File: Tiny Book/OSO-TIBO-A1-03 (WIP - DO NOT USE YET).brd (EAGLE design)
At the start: 54.9 x 88.1 mm, 106 parts, among them J2 10118193-0001LF, Q1 DMG341, Q2 IRLML0100, SW1 SPST_TACTILE_SWITCHRA-THRU, SW2 SPDT_SWITCH, U1 AP2112-3.3, U2 MCP73831T-2ACI/OT, U3 ATSAMD51G18A-MUT, U4 GD25Q16C (or GD25Q32C), U5 MAX4468EKAT, X1 JSTPH, X2 2x5 0.05" SWD

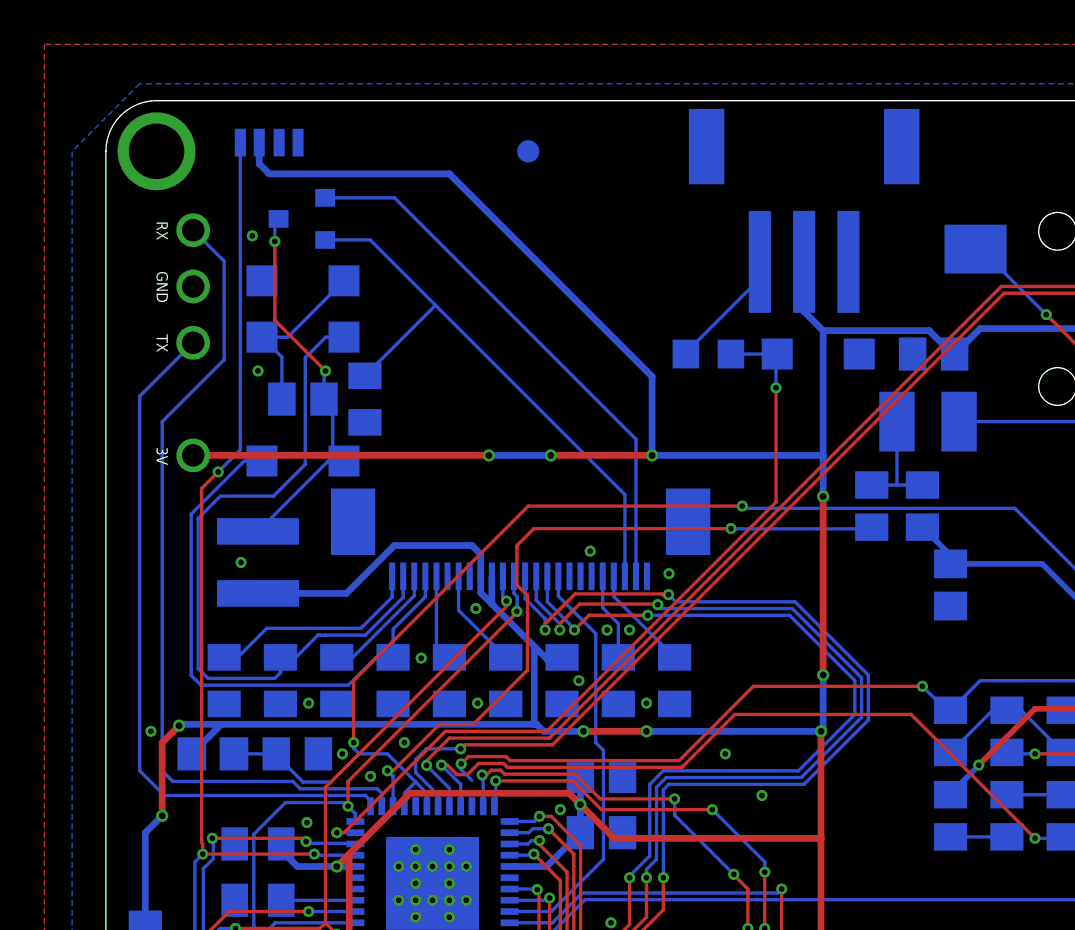
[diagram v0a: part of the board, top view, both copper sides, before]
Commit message: silkscreen and dimension tweaks
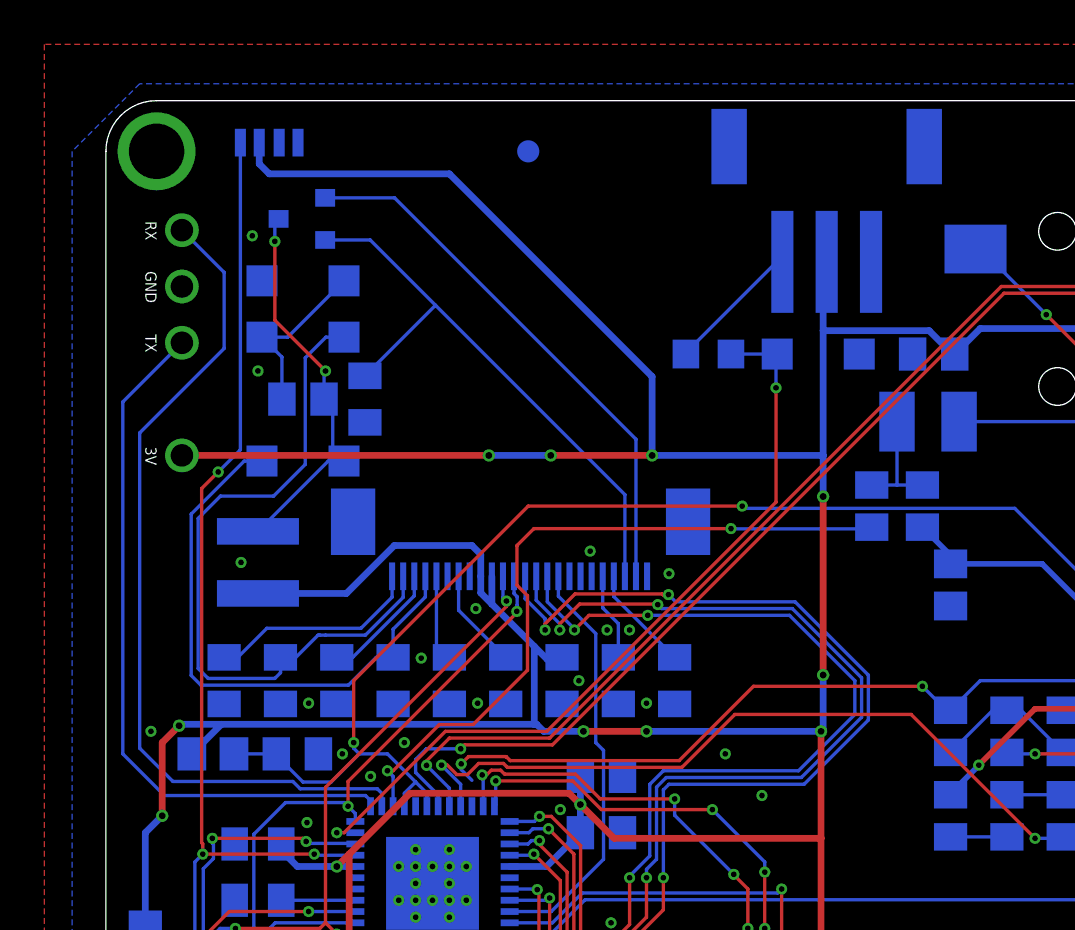
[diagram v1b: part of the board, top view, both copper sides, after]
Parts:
- moved ACCESSORY_PORT 1.02 mm to (32.5, 83.8)
- moved JP1 0.51 mm to (3.43, 80.0)
- moved JP2 0.51 mm to (3.43, 72.4)
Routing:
- net D0_SERCOM1_RX: track 37.0 -> 38.1 mm
- net _ACCESSORY: track 5.54 -> 6.11 mm
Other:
- board text added: "RX/TX=D1/D0=PA00/PA01"
- board text removed: "TX/RX=D1/D0=PA00/PA01"

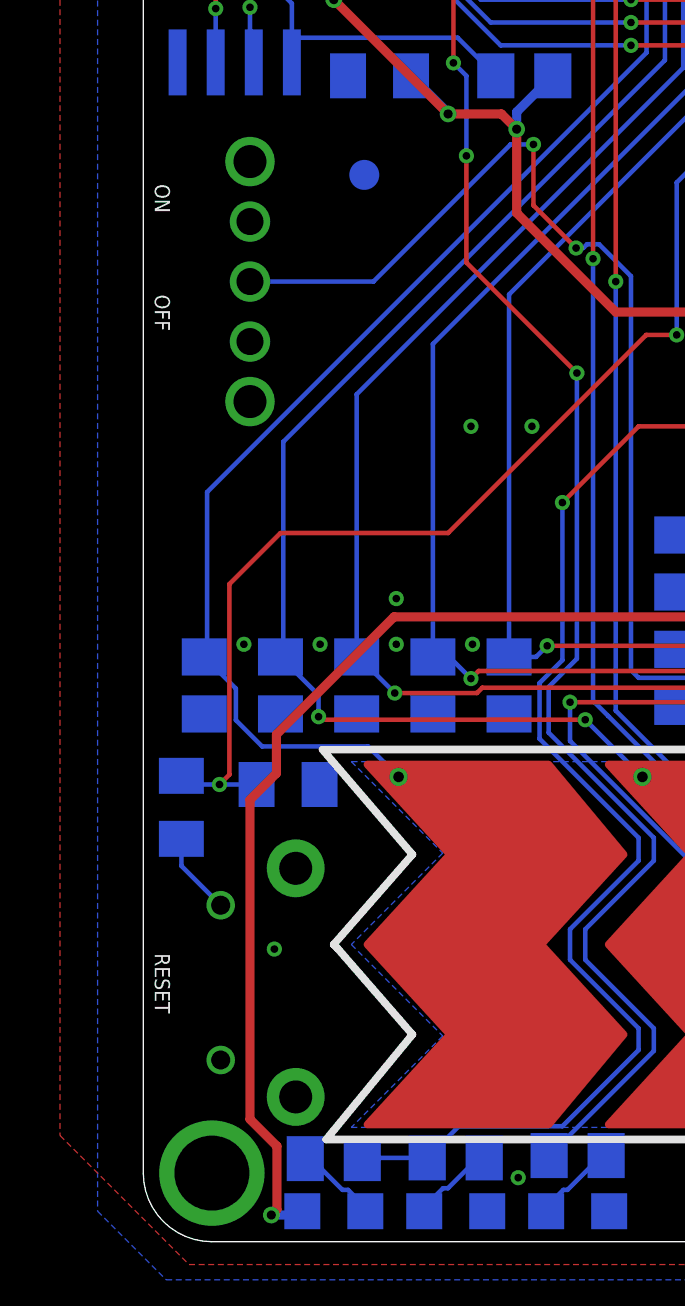
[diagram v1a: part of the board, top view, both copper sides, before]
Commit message: surface mount reset button
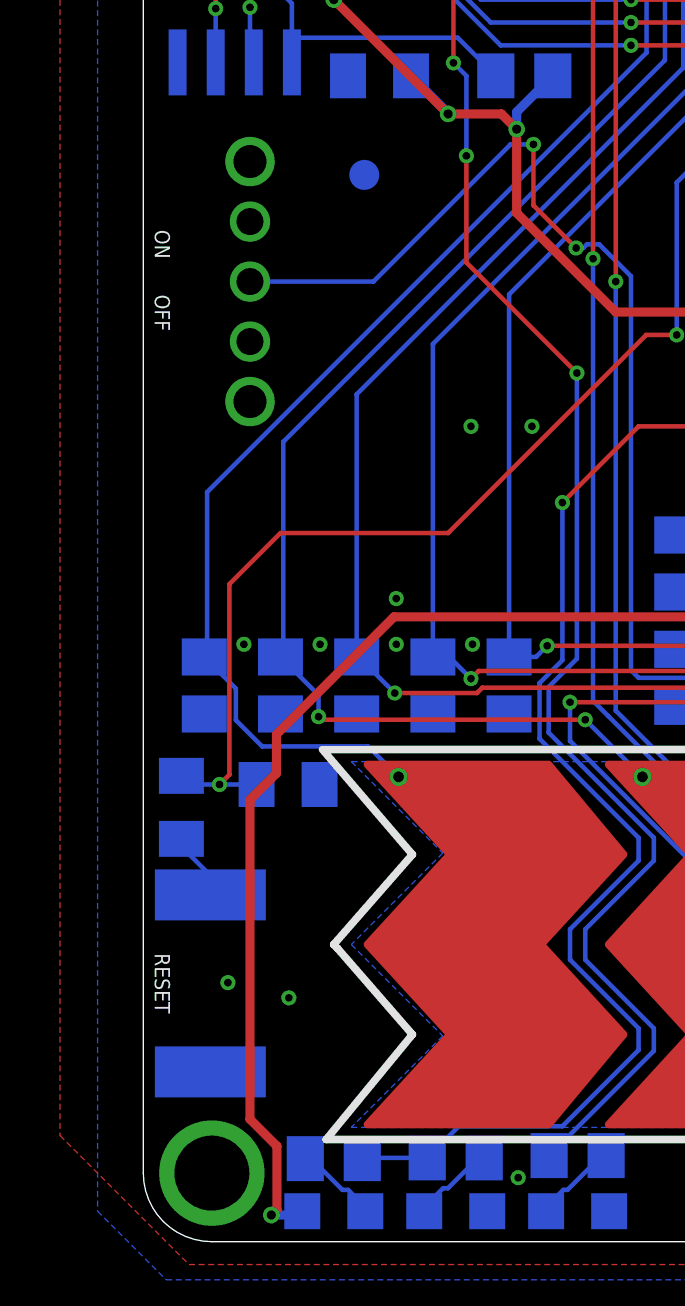
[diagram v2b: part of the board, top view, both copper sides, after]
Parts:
- removed SW1: SPST_TACTILE_SWITCHRA-THRU, My Stuff:MJTP1117
- added BTN_RESET: (no value), adafruit:BTN_CK_KSS
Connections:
- net GND: now also BTN_RESET.P$1; no longer SW1.P$1
- net N$1: now also BTN_RESET.P$2; no longer SW1.P$2
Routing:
- net GND: vias 61 -> 62
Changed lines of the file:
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@@
 lazer bear: adafru.it/4237</text>
 <text x="0.635" y="31.2166" size="0.508" layer="21" font="vector" ratio="18" rot="SR270" align="center">OFF</text>
-<text x="0.635" y="35.0266" size="0.508" layer="21" font="vector" ratio="18" rot="SR270" align="center">ON</text>
+<text x="0.635" y="33.5026" size="0.508" layer="21" font="vector" ratio="18" rot="SR270" align="center">ON</text>
 <text x="0.635" y="8.8646" size="0.508" layer="21" font="vector" ratio="18" rot="SR270" align="center">RESET</text>
 <wire x1="28.448" y1="16.51" x2="28.448" y2="11.938" width="0.1524" layer="22" style="shortdash"/>
@@
 </element>
 <element name="SW2" library="My Stuff" package="A10767" value="SPDT_SWITCH" x="3.556" y="32.258" smashed="yes" rot="MR90"/>
-<element name="SW1" library="My Stuff" package="MJTP1117" value="SPST_TACTILE_SWITCHRA-THRU" x="2.54" y="8.89" smashed="yes" rot="MR90"/>
 <element name="JP1" library="adafruit" package="1X03" value="" x="3.429" y="80.01" smashed="yes" rot="MR90">
 <attribute name="VALUE" x="0.254" y="76.2" size="1.27" layer="28" rot="MR90"/>
@@
 <attribute name="NAME" x="0.635" y="50.292" size="0.508" layer="26" font="vector" ratio="18" rot="MR90" align="center"/>
 <attribute name="VALUE" x="1.016" y="52.324" size="0.4064" layer="28" ratio="10" rot="MR90"/>
+</element>
+<element name="BTN_RESET" library="adafruit" package="BTN_CK_KSS" value="" x="2.2352" y="8.8646" smashed="yes" rot="MR90">
+<attribute name="NAME" x="4.826" y="8.89" size="0.508" layer="26" font="vector" ratio="18" rot="MR90" align="center"/>
+<attribute name="VALUE" x="3.3792" y="6.9786" size="0.4064" layer="28" ratio="10" rot="MR90"/>
 </element>
 </elements>
@@
 <contactref element="TP2" pad="P$1"/>
 <contactref element="LED" pad="C"/>
-<contactref element="SW1" pad="P$1"/>
 <contactref element="C11" pad="1"/>
 <contactref element="FUL" pad="C"/>
@@
 <via x="5.8928" y="20.1676" extent="1-16" drill="0.254"/>
 <via x="3.3528" y="20.1676" extent="1-16" drill="0.254"/>
-<via x="4.3688" y="10.0076" extent="1-16" drill="0.254"/>
+<via x="4.8514" y="8.382" extent="1-16" drill="0.254"/>
 <via x="12.954" y="27.432" extent="1-16" drill="0.254"/>
 <via x="20.4978" y="56.4134" extent="1-16" drill="0.254"/>
@@
 <via x="6.604" y="82.296" extent="1-16" drill="0.254"/>
 <via x="44.5008" y="58.42" extent="1-16" drill="0.254"/>
+<contactref element="BTN_RESET" pad="P$1"/>
+<via x="2.8194" y="8.89" extent="1-16" drill="0.254"/>
 </signal>
 <signal name="D9_EINK_CS">
@@
 <wire x1="22.352" y1="21.336" x2="21.778" y2="21.336" width="0.3048" layer="16"/>
 </signal>
-<signal name="N$1">
-<contactref element="SW1" pad="P$2"/>
-<contactref element="R7" pad="1"/>
-<wire x1="2.58" y1="11.47" x2="1.27" y2="12.78" width="0.1524" layer="16"/>
-<wire x1="1.27" y1="12.78" x2="1.27" y2="13.682" width="0.1524" layer="16"/>
-</signal>
 <signal name="N$9">
 <contactref element="R9" pad="1"/>
@@
 <wire x1="24.01330625" y1="47.12730625" x2="24.01330625" y2="46.8758625" width="0.1524" layer="16"/>
 </signal>
+<signal name="N$1">
+<contactref element="R7" pad="1"/>
+<contactref element="BTN_RESET" pad="P$2"/>
+<wire x1="1.27" y1="13.682" x2="1.27" y2="13.428" width="0.1524" layer="16"/>
+<wire x1="2.2352" y1="12.4628" x2="1.27" y2="13.428" width="0.1524" layer="16"/>
+<wire x1="2.2352" y1="12.4628" x2="2.2352" y2="11.8146" width="0.1524" layer="16"/>
+</signal>
 </signals>

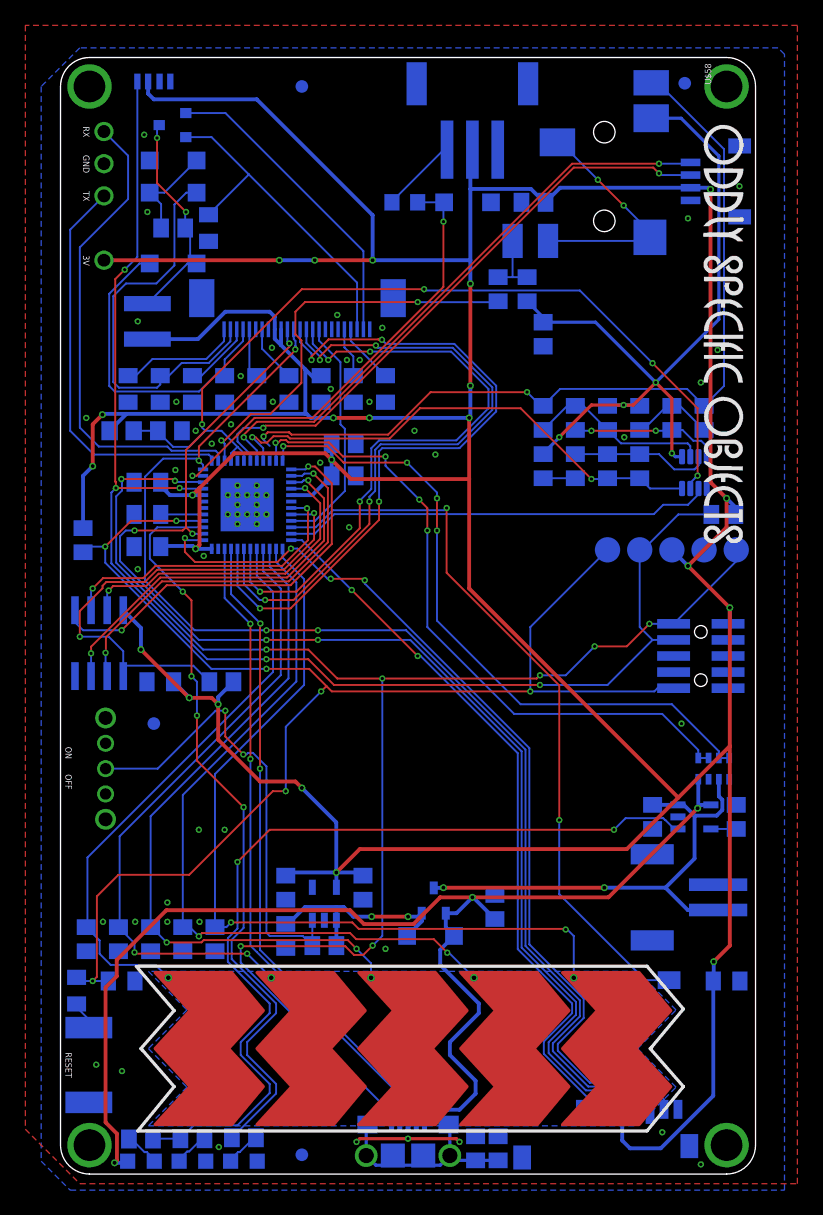
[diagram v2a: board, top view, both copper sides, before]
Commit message: route accessory and mic raw signals
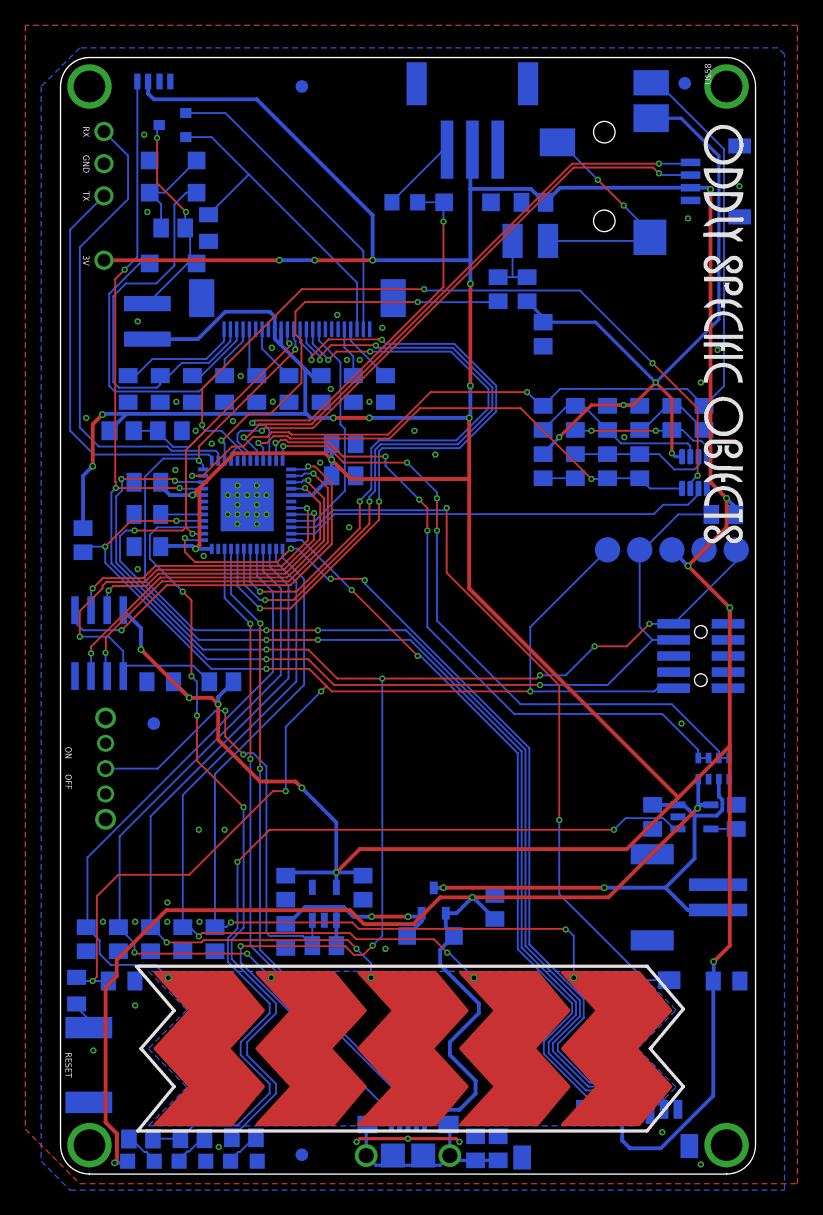
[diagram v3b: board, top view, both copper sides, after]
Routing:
- net D3_A1_MICRAW: track 67.7 -> 74.6 mm
- net D2_A3_ACCESSORY: track 34.8 -> 32.4 mm
- net A2_MICAMP: track 40.3 -> 39.0 mm
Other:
- board text added: "Audio out on A0/PA02; raw mic on D2/A3 /PB02 for inline btn presses."
- board text added: "I2C is a 4-pin JST-SH. SDA/SCL=D25/D26=PB08/ PB09. BYO pull-ups! Accessory port: 3-pin JST-PH on D3/A1/PA05."
- board text removed: "Audio out on A0/PA02; raw mic on D3/A1 /PA05 for inline btn presses."
- board text removed: "I2C is a 4-pin JST-SH. SDA/SCL=D25/D26=PB08/ PB09. BYO pull-ups! Accessory port: 3-pin JST-PH on D2/A3/PB02."

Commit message: use 4MB flash so babel can live there
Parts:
- U4: value GD25Q16C (or GD25Q32C) -> GD25Q32C
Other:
- board text added: "4MB FLASH CHIP"
- board text removed: "2MB FLASH CHIP"
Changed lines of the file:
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@@
         PA30 (it's way
         up top).</text>
-<text x="16.002" y="47.752" size="1.27" layer="22" font="vector" ratio="18" rot="MR0" align="top-left">2MB FLASH CHIP</text>
+<text x="16.002" y="47.752" size="1.27" layer="22" font="vector" ratio="18" rot="MR0" align="top-left">4MB FLASH CHIP</text>
 <wire x1="0.254" y1="48.26" x2="16.51" y2="48.26" width="0.1524" layer="22" style="shortdash"/>
 <text x="15.875" y="45.974" size="0.8128" layer="22" font="vector" rot="MR0" align="top-left">On a dedicated
@@
 <attribute name="BOM" value="EXCLUDE" x="19.05" y="86.106" size="1.778" layer="28" rot="MR270" display="off"/>
 </element>
-<element name="U4" library="Adafruit Feather M0 Express" package="MICROBUILDER_SOIC8_150MIL" value="GD25Q16C (or GD25Q32C)" x="3.048" y="42.164" smashed="yes" rot="MR0">
+<element name="U4" library="Adafruit Feather M0 Express" package="MICROBUILDER_SOIC8_150MIL" value="GD25Q32C" x="3.048" y="42.164" smashed="yes" rot="MR0">
 <attribute name="NAME" x="5.9182" y="42.799" size="0.508" layer="26" font="vector" ratio="18" rot="MR270" align="center"/>
 <attribute name="VALUE" x="4.953" y="41.783" size="0.508" layer="28" font="vector" ratio="18" rot="MR0" align="center"/>
